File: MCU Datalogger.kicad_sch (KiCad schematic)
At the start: 0 parts

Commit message: finish schematic process for MCU data logger
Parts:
- added BT1: Battery, Connector_PinHeader_2.54mm:PinHeader_1x02_P2.54mm_Vertical, symbol Device:Battery
- added C1, C4: 0.1uF, Capacitor_SMD:C_0805_2012Metric, symbol Device:C_US
- added C2, C3: 22pF, Capacitor_SMD:C_0805_2012Metric, symbol Device:C_US
- added C5: 100nF, Capacitor_SMD:C_0805_2012Metric, symbol Device:C_Polarized_Small_US
- added D1, D2: LED, LED_SMD:LED_0805_2012Metric, symbol Device:LED
- added H1, H2, H3, H4: MountingHole, MountingHole:MountingHole_2.1mm, symbol Mechanical:MountingHole
- added R1, R5: 330, Resistor_SMD:R_0805_2012Metric, symbol Device:R_US
- added R2, R6, R7: 10K, Resistor_SMD:R_0805_2012Metric, symbol Device:R_US
- added R3, R4: 4.7K, Resistor_SMD:R_0805_2012Metric, symbol Device:R_US
- added U1, U2: 24LC1025, Package_SO:SOIC-8_5.3x5.3mm_P1.27mm, symbol Memory_EEPROM:24LC1025
- added U3: DS1337S_, Footprints:SOIC127P600X175-8N, symbol DS1337S:DS1337S_
- added U4: ATMEGA328P-AU, Footprints:QFP80P900X900X120-32N, symbol ATMEGA328P:ATMEGA328P-AU
- added Y1: 32.768 KHz, Crystal:Crystal_SMD_5032-2Pin_5.0x3.2mm_HandSoldering, symbol Device:Crystal
- added Y2: 16 MHz, Crystal:Crystal_SMD_5032-2Pin_5.0x3.2mm_HandSoldering, symbol Device:Crystal
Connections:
- new net: C3.1, U4.8 (PB7), Y2.1
- new net: C2.1, U4.7 (PB6), Y2.2
- new net: U3.2 (X2), Y1.1
- new net: U3.1 (X1), Y1.2
- new net: R7.2, U3.7 (SQW/~INT)
- new net: R6.2, U3.3 (~{INTA})
- new net: D1.1 (K), R5.2
- new net: D2.1 (K), R1.1
- new net: C4.1, U4.20 (AREF)
- new net D2: U4.32 (PD2)
- new net D3: U4.1 (PD3)
- new net D4: U4.2 (PD4)
- new net D5: U4.9 (PD5)
- new net D6: U4.10 (PD6)
- new net D7: U4.11 (PD7)
- new net D8: U4.12 (PB0)
- new net GND: BT1.2 (-), C1.2, C2.2, C3.2, C4.2, C5.2, R1.2, R5.1, U1.4 (GND), U1.7 (WP), U2.2 (A1), U2.4 (GND), U2.7 (WP), U3.4 (GND), U4.21 (GND), U4.3 (GND), U4.5 (GND)
- new net MISO: U4.16 (PB4)
- new net MOSI: U4.15 (PB3)
- new net RESET: R2.2, U4.29 (PC6/~{RESET})
- new net RX: U4.30 (PD0)
- new net SCK: D1.2 (A), R3.2, U1.6 (SCL), U2.6 (SCL), U3.6 (SCL), U4.17 (PB5), U4.28 (PC5)
- new net SDA: R4.2, U1.5 (SDA), U2.5 (SDA), U3.5 (SDA), U4.27 (PC4)
- new net TX: U4.31 (PD1)
- new net Vcc: BT1.1 (+), C1.1, C5.1, D2.2 (A), R2.1, R3.1, R4.1, R6.1, R7.1, U1.1 (A0), U1.2 (A1), U1.3 (A2), U1.8 (VCC), U2.1 (A0), U2.3 (A2), U2.8 (VCC), U3.8 (VCC), U4.18 (AVCC), U4.4 (VCC)
- no-connect marks 0 -> 9
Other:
- added sheet Connectors (Connectors.kicad_sch)
- note added: "Atmega Micro Control Circuit"
- note added: "EEPROM Memory"
- note added: "Mounting"
- note added: "Real time clock circuit"
- company: (none) -> Evan Stewart
- title: (none) -> ${project_name}

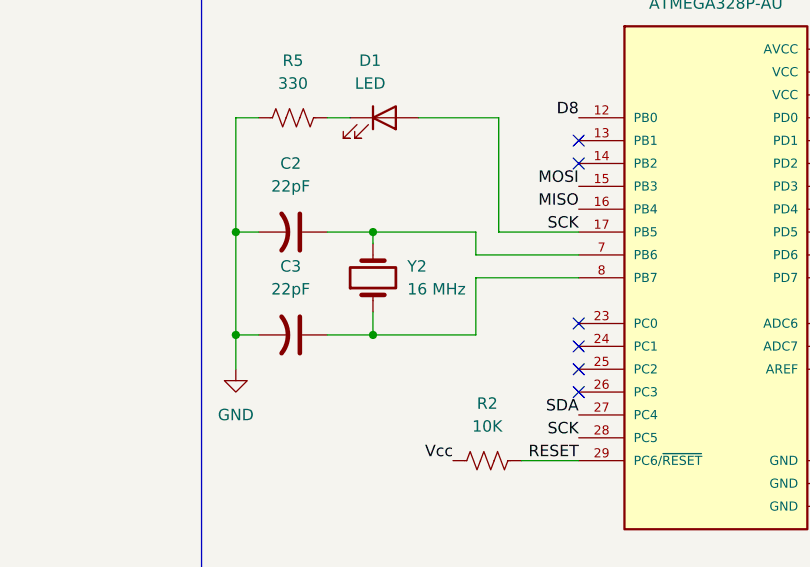
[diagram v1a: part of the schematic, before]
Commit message: Re-design 2 layer board
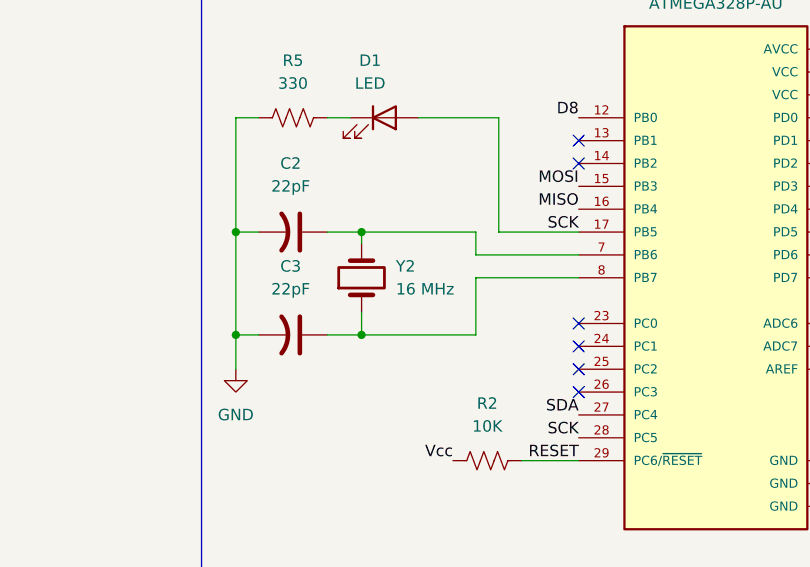
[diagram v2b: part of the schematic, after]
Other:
- moved on the sheet: Y2
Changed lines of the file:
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@@
-	)
-	(junction
-		(at 167.64 60.96)
-		(diameter 0)
-		(color 0 0 0 0)
 	)
 	(junction
@@
 	)
 	(junction
+		(at 166.37 60.96)
+		(diameter 0)
+		(color 0 0 0 0)
+	)
+	(junction
 		(at 152.4 60.96)
 		(diameter 0)
@@
 	)
 	(junction
-		(at 167.64 72.39)
-		(diameter 0)
-		(color 0 0 0 0)
-	)
-	(junction
 		(at 152.4 72.39)
+		(diameter 0)
+		(color 0 0 0 0)
+	)
+	(junction
+		(at 166.37 72.39)
 		(diameter 0)
 		(color 0 0 0 0)
@@
 	(wire
 		(pts
-			(xy 179.07 72.39) (xy 167.64 72.39)
-		)
-		(stroke
-			(width 0)
-			(type default)
-		)
-	)
-	(wire
-		(pts
 			(xy 190.5 66.04) (xy 179.07 66.04)
 		)
@@
 	(wire
 		(pts
-			(xy 179.07 60.96) (xy 167.64 60.96)
-		)
-		(stroke
-			(width 0)
-			(type default)
-		)
-	)
-	(wire
-		(pts
 			(xy 233.68 76.2) (xy 233.68 88.9)
 		)
@@
 	(wire
 		(pts
-			(xy 167.64 62.23) (xy 167.64 60.96)
+			(xy 166.37 62.23) (xy 166.37 60.96)
 		)
 		(stroke
@@
 	(wire
 		(pts
-			(xy 162.56 72.39) (xy 167.64 72.39)
+			(xy 166.37 60.96) (xy 179.07 60.96)
+		)
+		(stroke
+			(width 0)
+			(type default)
+		)
+	)
+	(wire
+		(pts
+			(xy 162.56 72.39) (xy 166.37 72.39)
 		)
 		(stroke
@@
 	(wire
 		(pts
-			(xy 167.64 72.39) (xy 167.64 69.85)
+			(xy 166.37 72.39) (xy 166.37 69.85)
 		)
 		(stroke
@@
 	(wire
 		(pts
-			(xy 162.56 60.96) (xy 167.64 60.96)
+			(xy 166.37 72.39) (xy 179.07 72.39)
+		)
+		(stroke
+			(width 0)
+			(type default)
+		)
+	)
+	(wire
+		(pts
+			(xy 162.56 60.96) (xy 166.37 60.96)
 		)
 		(stroke
@@
 	(symbol
 		(lib_id "Device:Crystal")
-		(at 167.64 66.04 90)
+		(at 166.37 66.04 90)
 		(unit 1)
 		(exclude_from_sim no)
@@
 		(fields_autoplaced yes)
 		(property "Reference" "Y2"
-			(at 171.45 64.7699 90)
+			(at 170.18 64.7699 90)
 			(effects
 				(font
@@
 		)
 		(property "Value" "16 MHz"
-			(at 171.45 67.3099 90)
+			(at 170.18 67.3099 90)
 			(effects
 				(font
@@
 		)
 		(property "Footprint" "Crystal:Crystal_SMD_5032-2Pin_5.0x3.2mm_HandSoldering"
-			(at 167.64 66.04 0)
+			(at 166.37 66.04 0)
 			(effects
 				(font
@@
 		)
 		(property "Datasheet" "~"
-			(at 167.64 66.04 0)
+			(at 166.37 66.04 0)
 			(effects
 				(font
@@
 		)
 		(property "Description" "Two pin crystal"
-			(at 167.64 66.04 0)
+			(at 166.37 66.04 0)
 			(effects
 				(font
@@
 		)
 		(property "Purpose" ""
-			(at 167.64 66.04 0)
+			(at 166.37 66.04 0)
 			(effects
 				(font

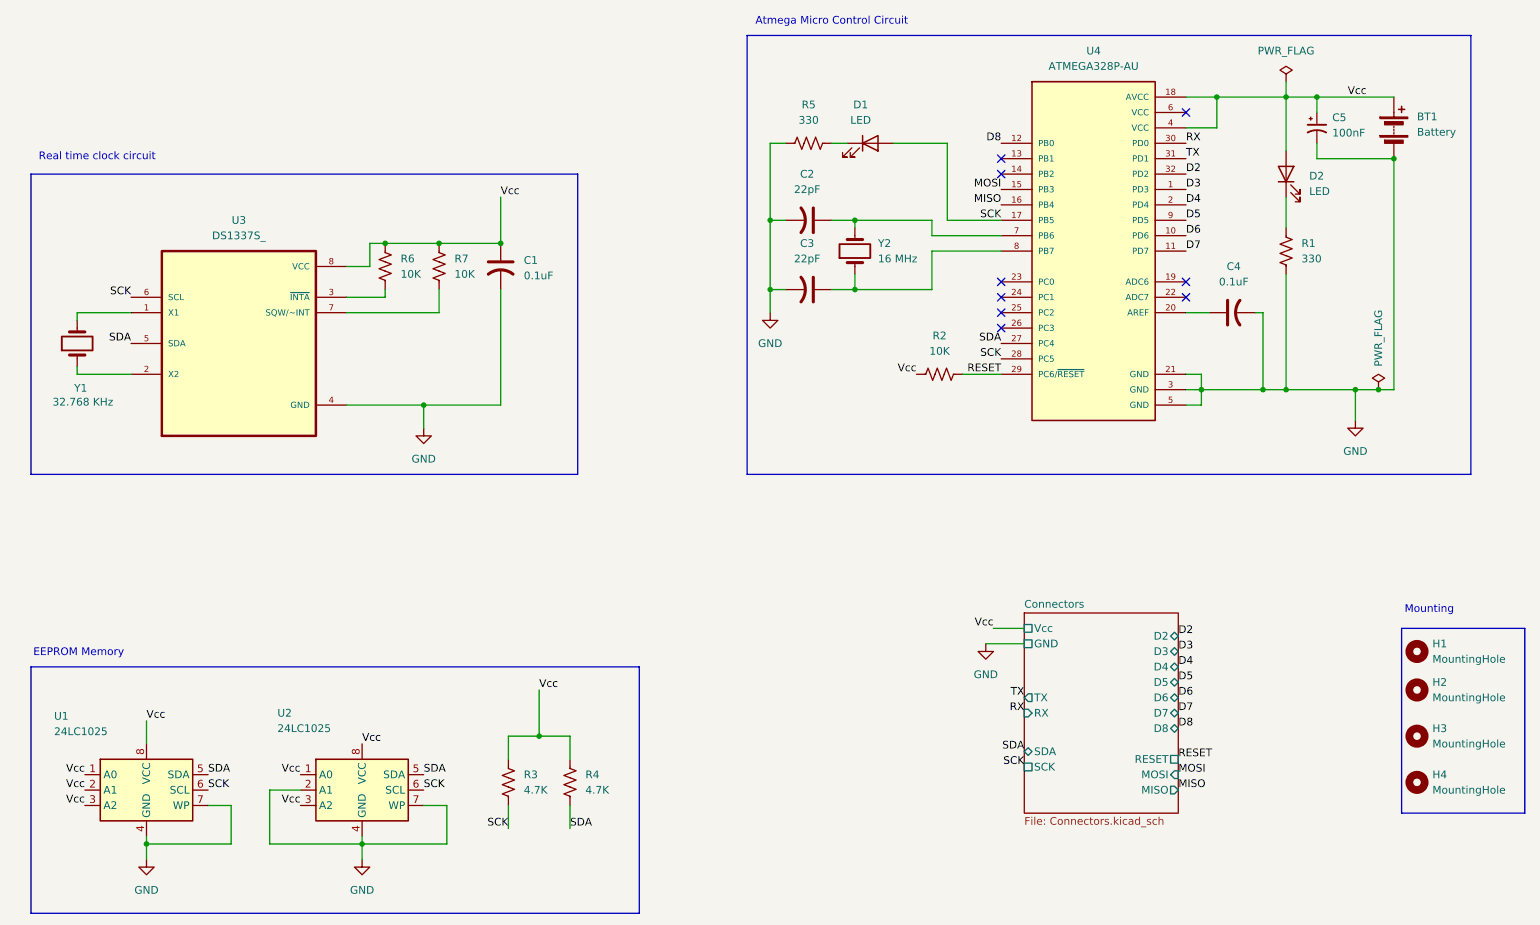
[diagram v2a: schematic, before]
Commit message: Fix Clock Bug
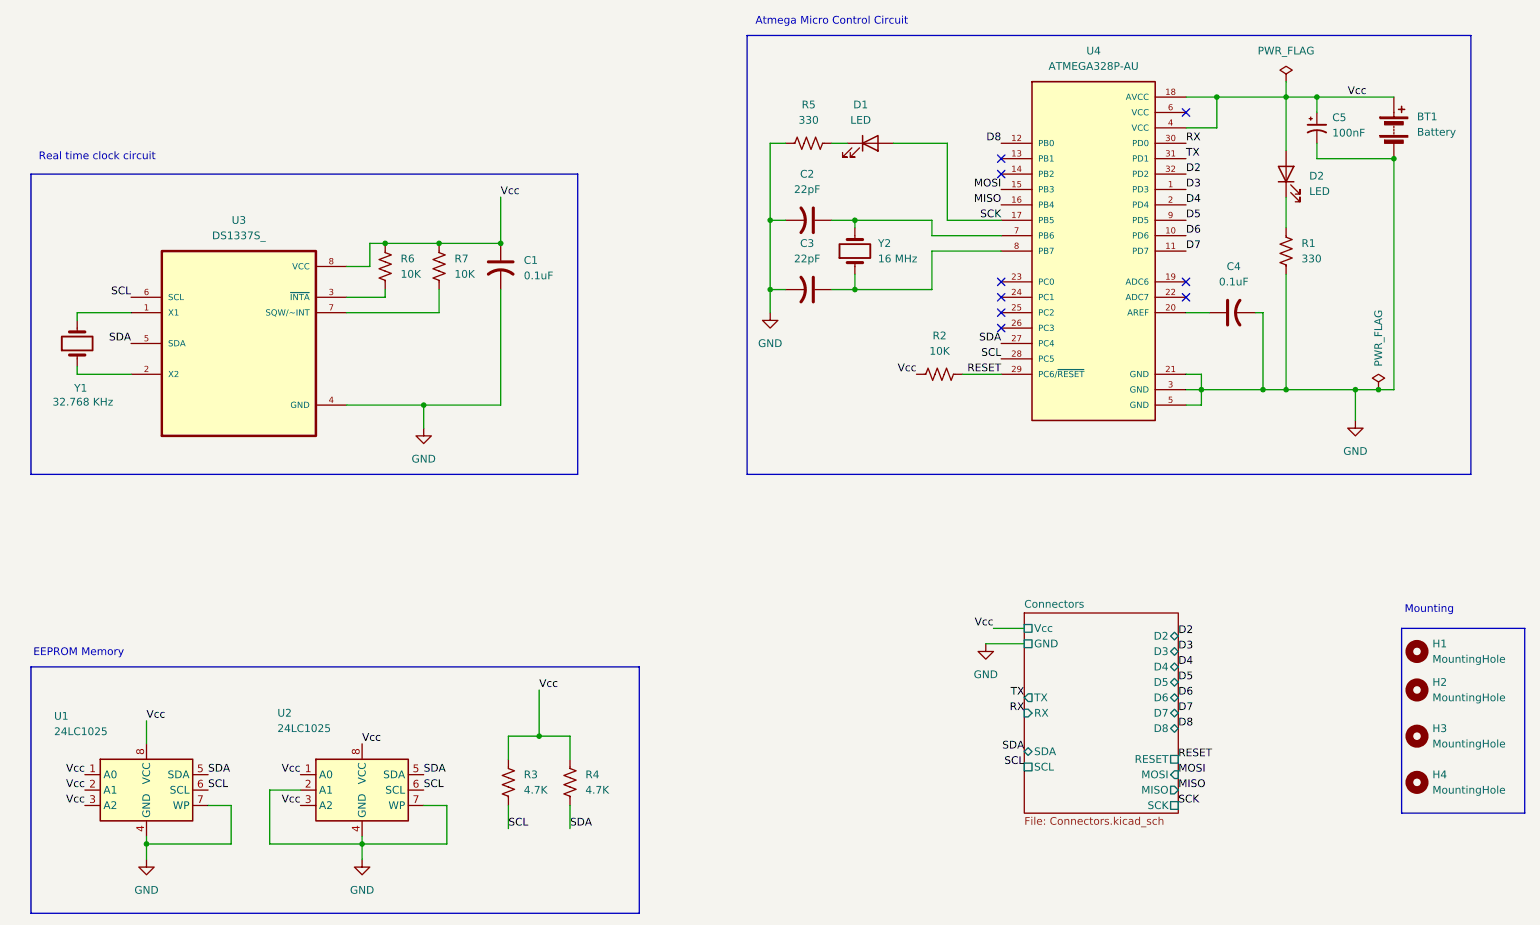
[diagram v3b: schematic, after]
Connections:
- net SCK: no longer R3.2, U1.6 (SCL), U2.6 (SCL), U3.6 (SCL), U4.28 (PC5)
- new net SCL: R3.2, U1.6 (SCL), U2.6 (SCL), U3.6 (SCL), U4.28 (PC5)
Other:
- sheet Connectors ports: added SCL; removed none
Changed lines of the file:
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@@
 		)
 	)
-	(label "SCK"
-		(at 46.99 73.66 180)
-		(effects
-			(font
-				(size 1.27 1.27)
-			)
-			(justify right bottom)
-		)
-	)
 	(label "TX"
 		(at 220.98 50.8 0)
@@
 		)
 	)
+	(label "SCL"
+		(at 95.25 154.94 0)
+		(effects
+			(font
+				(size 1.27 1.27)
+			)
+			(justify left bottom)
+		)
+	)
 	(label "Vcc"
 		(at 74.93 157.48 180)
@@
 		)
 	)
-	(label "SCK"
-		(at 109.22 161.29 180)
+	(label "SCL"
+		(at 46.99 73.66 180)
 		(effects
 			(font
@@
 		)
 	)
-	(label "SCK"
+	(label "SCL"
 		(at 190.5 83.82 180)
 		(effects
@@
 		)
 	)
+	(label "SCL"
+		(at 109.22 161.29 0)
+		(effects
+			(font
+				(size 1.27 1.27)
+			)
+			(justify left bottom)
+		)
+	)
 	(label "Vcc"
 		(at 49.53 143.51 0)
@@
 		)
 	)
+	(label "SCK"
+		(at 219.71 157.48 0)
+		(effects
+			(font
+				(size 1.27 1.27)
+			)
+			(justify left bottom)
+		)
+	)
 	(label "D8"
 		(at 190.5 48.26 180)
@@
 		)
 	)
+	(label "SCL"
+		(at 59.69 154.94 0)
+		(effects
+			(font
+				(size 1.27 1.27)
+			)
+			(justify left bottom)
+		)
+	)
 	(label "D8"
 		(at 219.71 144.78 0)
@@
 		)
 	)
-	(label "SDA"
-		(at 194.31 148.59 180)
+	(label "SCL"
+		(at 194.31 151.13 180)
 		(effects
 			(font
@@
 		)
 	)
-	(label "SCK"
-		(at 59.69 154.94 0)
+	(label "SDA"
+		(at 194.31 148.59 180)
 		(effects
 			(font
 				(size 1.27 1.27)
 			)
-			(justify left bottom)
+			(justify right bottom)
 		)
 	)
@@
 		)
 	)
-	(label "SCK"
-		(at 95.25 154.94 0)
-		(effects
-			(font
-				(size 1.27 1.27)
-			)
-			(justify left bottom)
-		)
-	)
-	(label "SCK"
-		(at 194.31 151.13 180)
-		(effects
-			(font
-				(size 1.27 1.27)
-			)
-			(justify right bottom)
-		)
-	)
 	(symbol
 		(lib_id "Device:Crystal")
@@
 			)
 		)
-		(pin "SCK" passive
+		(pin "SCL" passive
 			(at 194.31 151.13 180)
 			(effects
@@
 			)
 		)
+		(pin "SCK" passive
+			(at 219.71 157.48 0)
+			(effects
+				(font
+					(size 1.27 1.27)
+				)
+				(justify right)
+			)
+		)
